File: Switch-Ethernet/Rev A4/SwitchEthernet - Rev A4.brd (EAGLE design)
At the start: 86 x 90 mm, 121 parts, among them J1 22-05-7028-02, J2 DF17(4.0)-20DS-0.5V(57), J3 DF17(4.0)-20DP-0.5V(57), P1 RB1-125BAG1A, T1 H1102FNL, T2 H1102FNL, T3 EXMACHINA-LOGO-NAME, U1 TC1264-3.3, U2 TC1264-1.8, U3 KSZ8995MA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

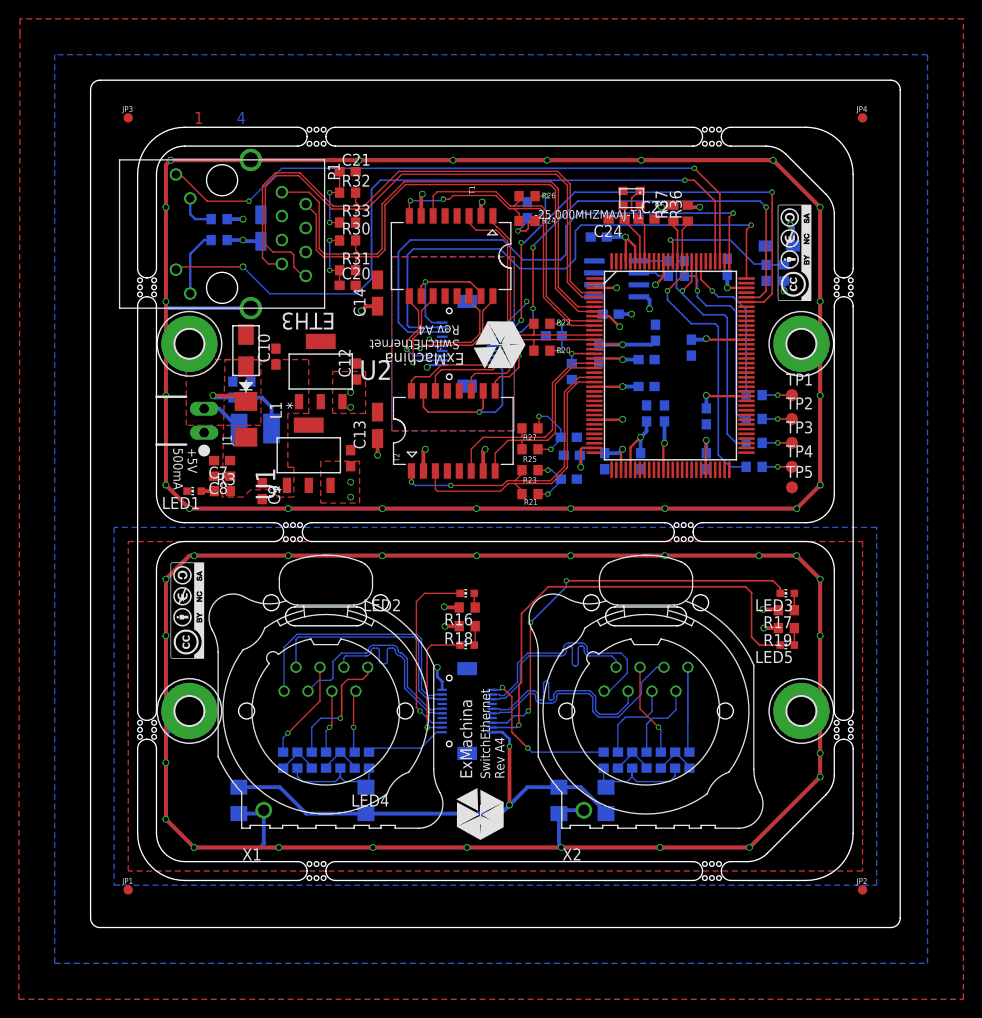
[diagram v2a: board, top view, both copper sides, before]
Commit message: Place name and value correctly on the board
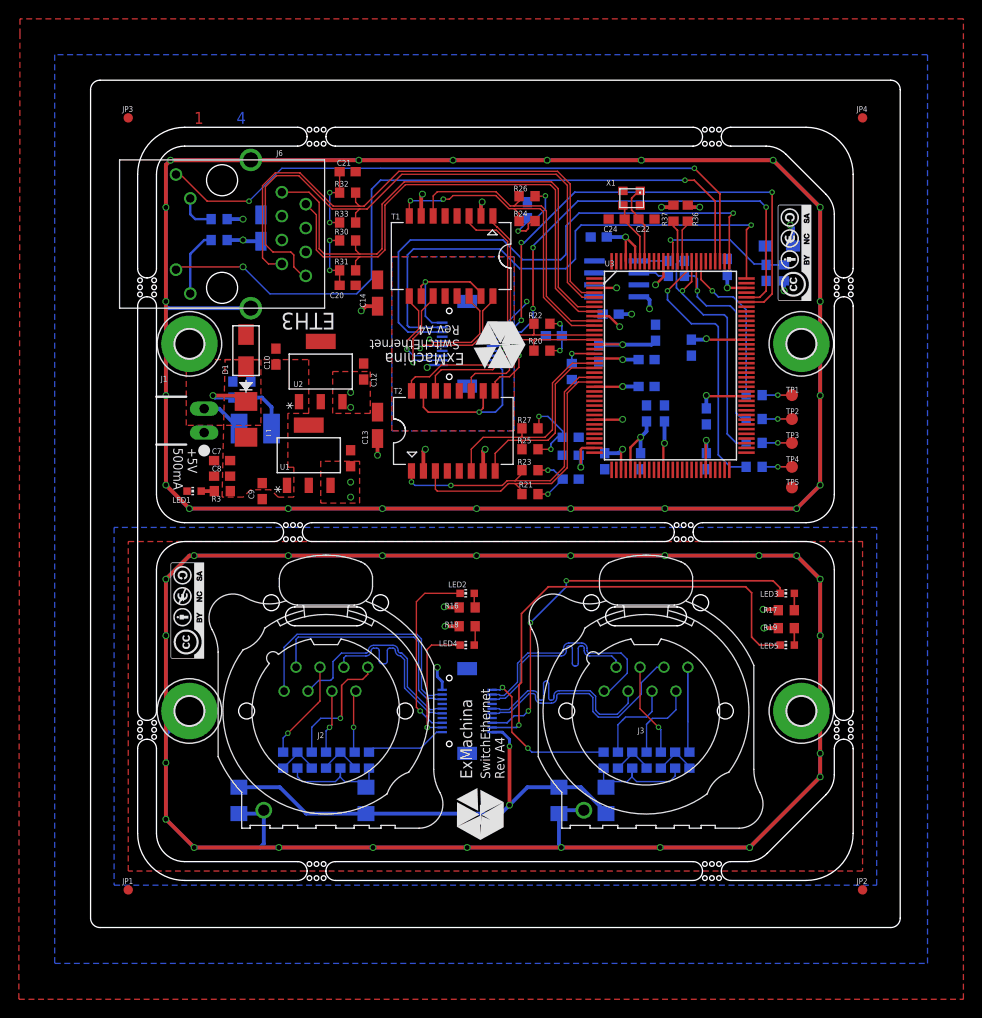
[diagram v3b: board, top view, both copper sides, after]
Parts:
- removed -25.000MHZMAAJ-T1: 8Z-25.000MHZMAAJ-T, crystal:SMD2.5X2
- removed CR1: SMAJ33A-E3/61, diode:DIODE_DO-214AC
- removed X2: NE8FAV, con-neutrik_ag:NE8FAV
- added D2: 1N4148WS, diode:SOD323-W
- added J4: DF17(4.0)-20DS-0.5V(57), con-hirose:DF17-20DS
- added J5: DF17(4.0)-20DP-0.5V(57), con-hirose:DF17-20DP
- D1: value 1N4148WS -> SMAJ33A-E3/61; device diode:SOD323-W -> diode:DIODE_DO-214AC
- J2: value DF17(4.0)-20DS-0.5V(57) -> NE8FAV; device con-hirose:DF17-20DS -> con-neutrik_ag:NE8FAV
- J3: value DF17(4.0)-20DP-0.5V(57) -> NE8FAV; device con-hirose:DF17-20DP -> con-neutrik_ag:NE8FAV
- X1: value NE8FAV -> 8Z-25.000MHZMAAJ-T; device con-neutrik_ag:NE8FAV -> crystal:SMD2.5X2
- moved X1 63.4 mm to (57.5, 77.5), turned to 180 degrees
- moved D1 57.7 mm to (16.5, 61.3), flipped to the top, turned to 90 degrees
- moved J3 43.4 mm to (59.0, 23.0), flipped to the top, turned to 0 degrees
- moved J2 15.0 mm to (25.0, 23.0), flipped to the top, turned to 0 degrees
- moved C12 0.75 mm to (29.0, 59.1)
- moved C16 0.20 mm to (51.0, 47.6)
- moved C18 0.20 mm to (51.0, 52.1)
- moved C27 0.12 mm to (51.0, 50.2)
- renumbered P1 to J6
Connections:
- net +3V3: now also D2.C, J4.1, J5.1; no longer D1.C, J2.1, J3.1
- net AGND: now also J2.G, J3.G; no longer X1.G, X2.G
- net CT_1: now also J4.10, J5.10; no longer J2.10, J3.10
- net CT_2: now also J4.11, J5.11; no longer J2.11, J3.11
- net GND: now also D1.2, J4.20, J5.20, X1.2, X1.4; no longer -25.000MHZMAAJ-T1.2, -25.000MHZMAAJ-T1.4, CR1.2, J2.20, J3.20
- net L1-1: now also J4.8, J5.8; no longer J2.8, J3.8
- net L1-2: now also J4.9, J5.9; no longer J2.9, J3.9
- net L2-1: now also J4.18, J5.18; no longer J2.18, J3.18
- net L2-2: now also J4.19, J5.19; no longer J2.19, J3.19
- net N$11: now also J2.5; no longer X1.5
- net N$12: now also J3.7; no longer X2.7
- net N$15: now also J3.4; no longer X2.4
- net N$18: now also J3.5; no longer X2.5
- net N$5: now also J3.8; no longer X2.8
- net N$7: now also J2.4; no longer X1.4
- net N$8: now also J2.8; no longer X1.8
- net N$9: now also J2.7; no longer X1.7
- net PW: now also D1.1; no longer CR1.1
- net RST_N: now also D2.A; no longer D1.A
- net RX1_N: now also J2.2, J4.3, J5.3; no longer J2.3, J3.3, X1.2
- net RX1_P: now also J2.1, J4.2, J5.2; no longer J2.2, J3.2, X1.1
- net RX2_N: now also J3.2, J4.13, J5.13; no longer J2.13, J3.13, X2.2
- net RX2_P: now also J3.1, J4.12, J5.12; no longer J2.12, J3.12, X2.1
- net TX1_N: now also J4.6, J5.6; no longer J3.6, X1.6
- net TX1_P: now also J2.3, J4.5, J5.5; no longer J2.5, J3.5, X1.3
- net TX2_N: now also J3.6, J4.16, J5.16; no longer J2.16, J3.16, X2.6
- net TX2_P: now also J3.3, J4.15, J5.15; no longer J2.15, J3.15, X2.3
- net X1: now also X1.1; no longer -25.000MHZMAAJ-T1.1
- net X2: now also X1.3; no longer -25.000MHZMAAJ-T1.3
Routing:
- net N$40: track 6.03 -> 6.74 mm
- net N$41: track 8.14 -> 8.64 mm
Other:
- board text removed: "+1V8"
- board text removed: "+5V"

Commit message: Generate MDP
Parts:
- added U$5: (no value), frames:A5L-LOC
